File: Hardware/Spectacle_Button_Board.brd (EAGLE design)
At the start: 34.3 x 62.2 mm, 40 parts, among them J19 FTDI_DEVICE, U1 CY8C4146LQI-S422, U2 MIC5205-5V

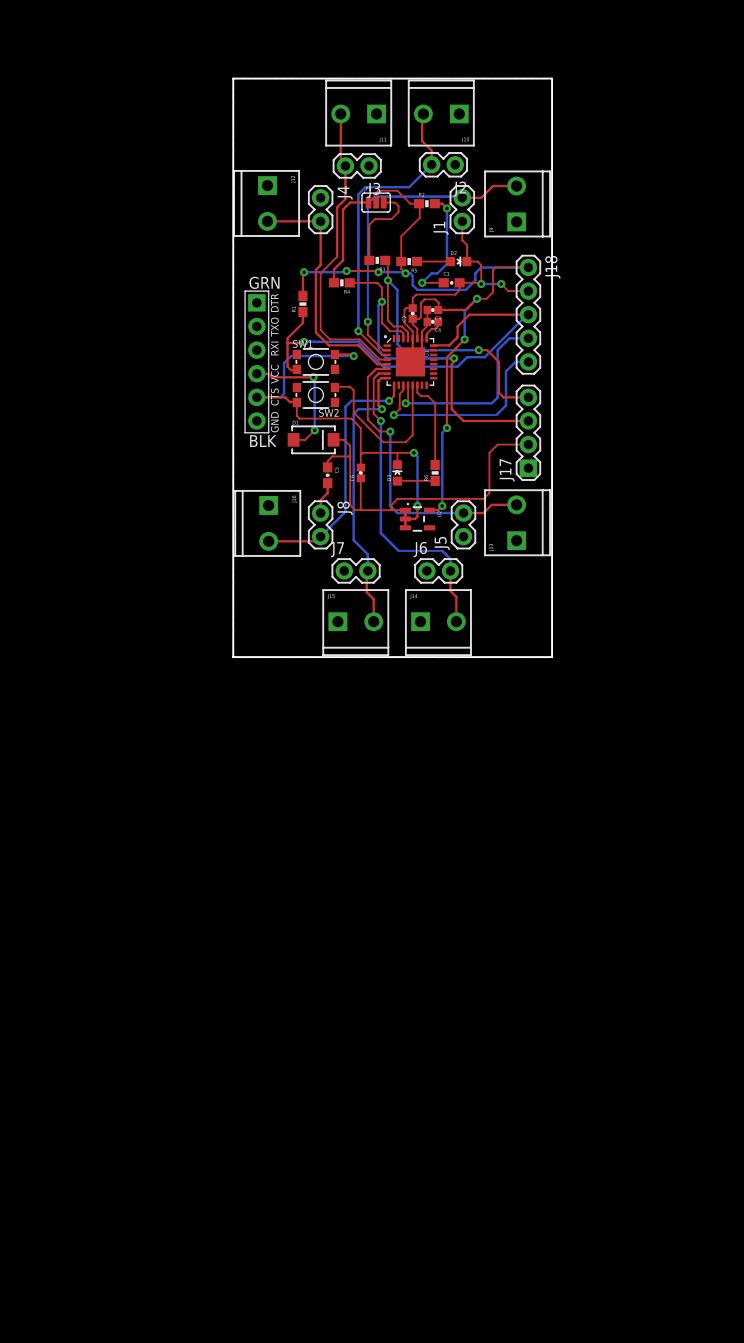
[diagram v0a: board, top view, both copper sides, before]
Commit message: Make some chgs (see full msg) - Add TVS diodes to all button and data/power lines - Partition schematic according to function - Change power/data connector to TRRS
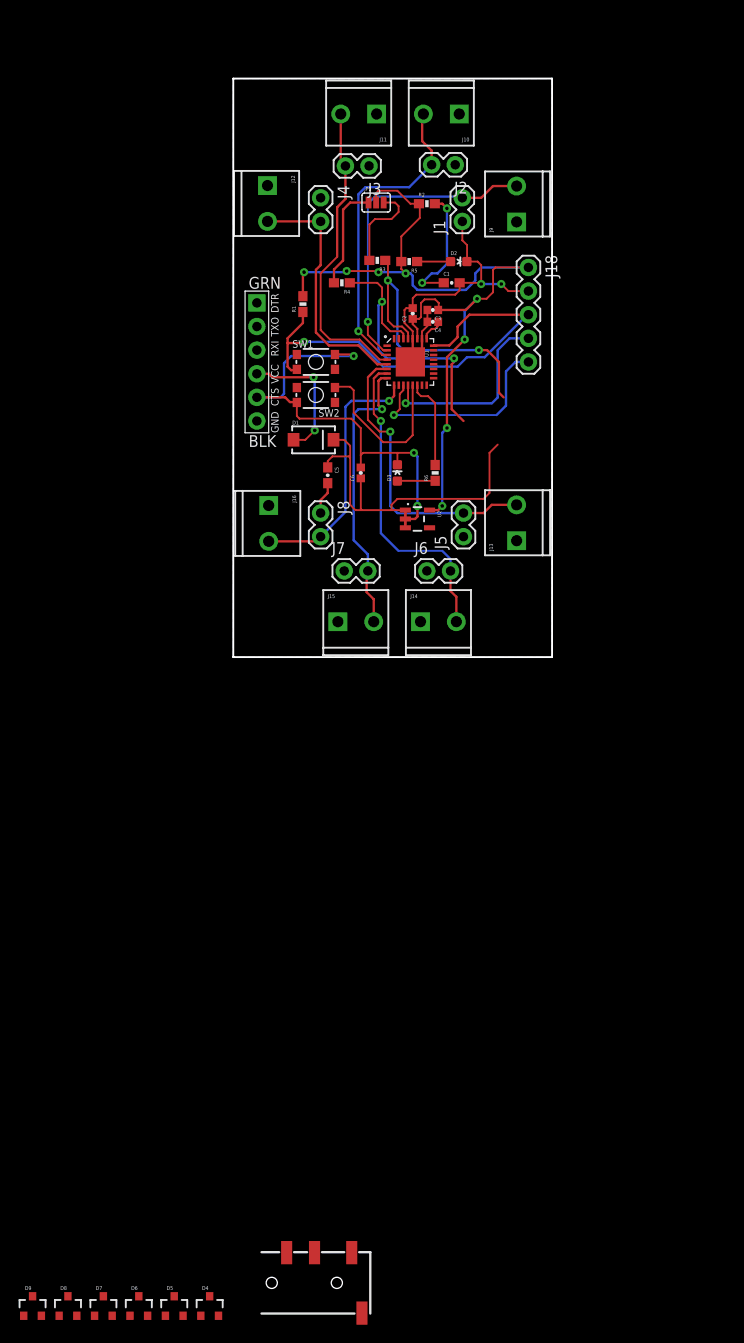
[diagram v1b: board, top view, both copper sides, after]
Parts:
- added D4, D5, D6, D7, D8, D9: PESD1CAN, SparkFun-DiscreteSemi:SOT23-3
- J17: value (none) -> AUDIO-JACK3; device SparkFun-Connectors:1X04 -> SparkFun-Connectors:AUDIO-JACK-TRRS-SMD
- moved J17 92.4 mm to (-24.1, -71.1), turned to 0 degrees
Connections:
- net GND: now also D4.3, D5.3, D6.3, D7.3, D8.3, D9.3, J17.RING2; no longer J17.1
- net IN_0: now also D6.2
- net IN_1: now also D6.1
- net IN_2: now also D8.2
- net IN_3: now also D8.1
- net IN_4: now also D7.2
- net IN_5: now also D7.1
- net IN_6: now also D9.2
- net IN_7: now also D9.1
- net SCL: now also D4.1, J17.RING1; no longer J17.4
- net SDA: now also D4.2, J17.TIP; no longer J17.3
- net VIN: now also D5.1, J17.EARTH; no longer J17.2
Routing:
- net SDA: track 39.0 -> 32.0 mm
- net VIN: track 43.8 -> 40.5 mm
- net SCL: track 35.6 -> 33.0 mm

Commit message: Fix TX and RX net names
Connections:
- removed net RX: U1.21
- removed net TX: U1.22
- net RXI: now also U1.21
- net TXO: now also U1.22
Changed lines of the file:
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@@
 <signal name="TXO">
 <contactref element="J19" pad="P$2"/>
+<contactref element="U1" pad="22"/>
+<wire x1="-24.13" y1="31.75" x2="-5.12" y2="28.69" width="0" layer="19" extent="1-1"/>
 </signal>
 <signal name="RXI">
 <contactref element="J19" pad="P$3"/>
-</signal>
-<signal name="RX">
 <contactref element="U1" pad="21"/>
-</signal>
-<signal name="TX">
-<contactref element="U1" pad="22"/>
+<wire x1="-24.13" y1="29.21" x2="-5.12" y2="28.19" width="0" layer="19" extent="1-1"/>
 </signal>
 <signal name="N$4">

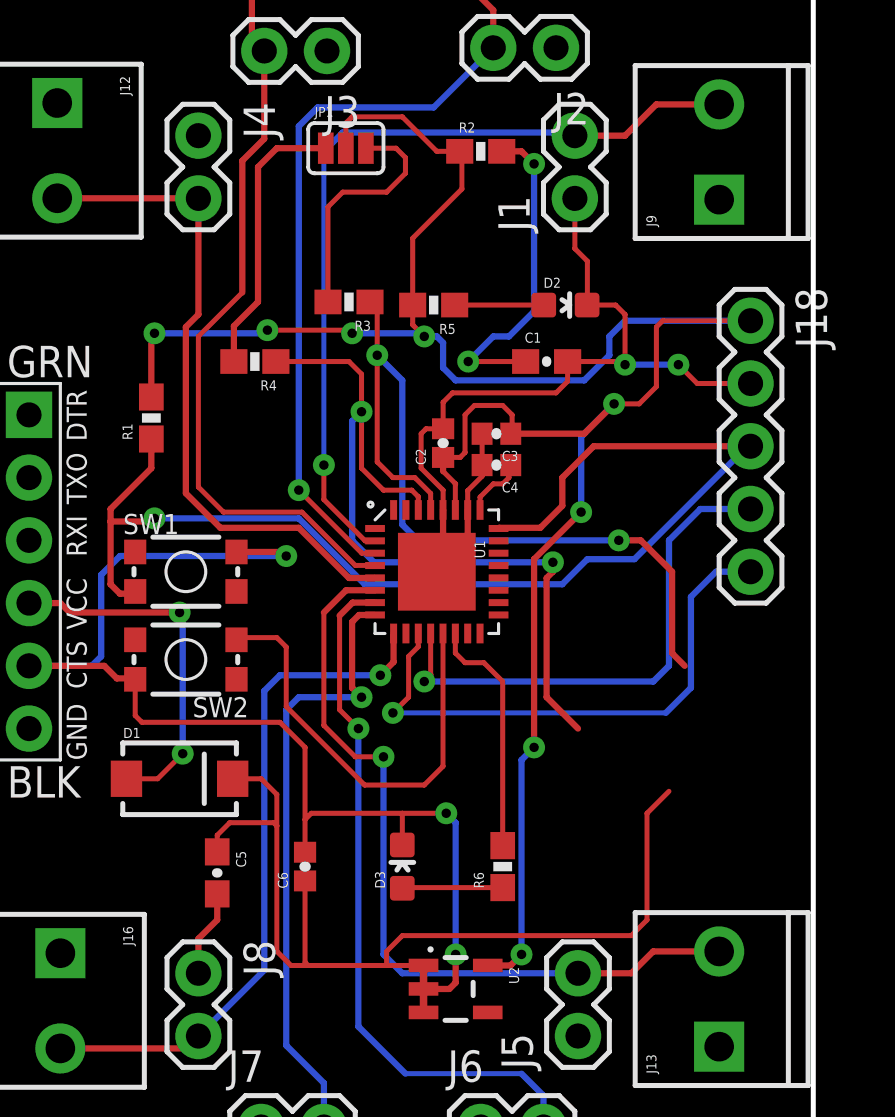
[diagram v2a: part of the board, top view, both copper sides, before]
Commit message: Adjust to 3.3V
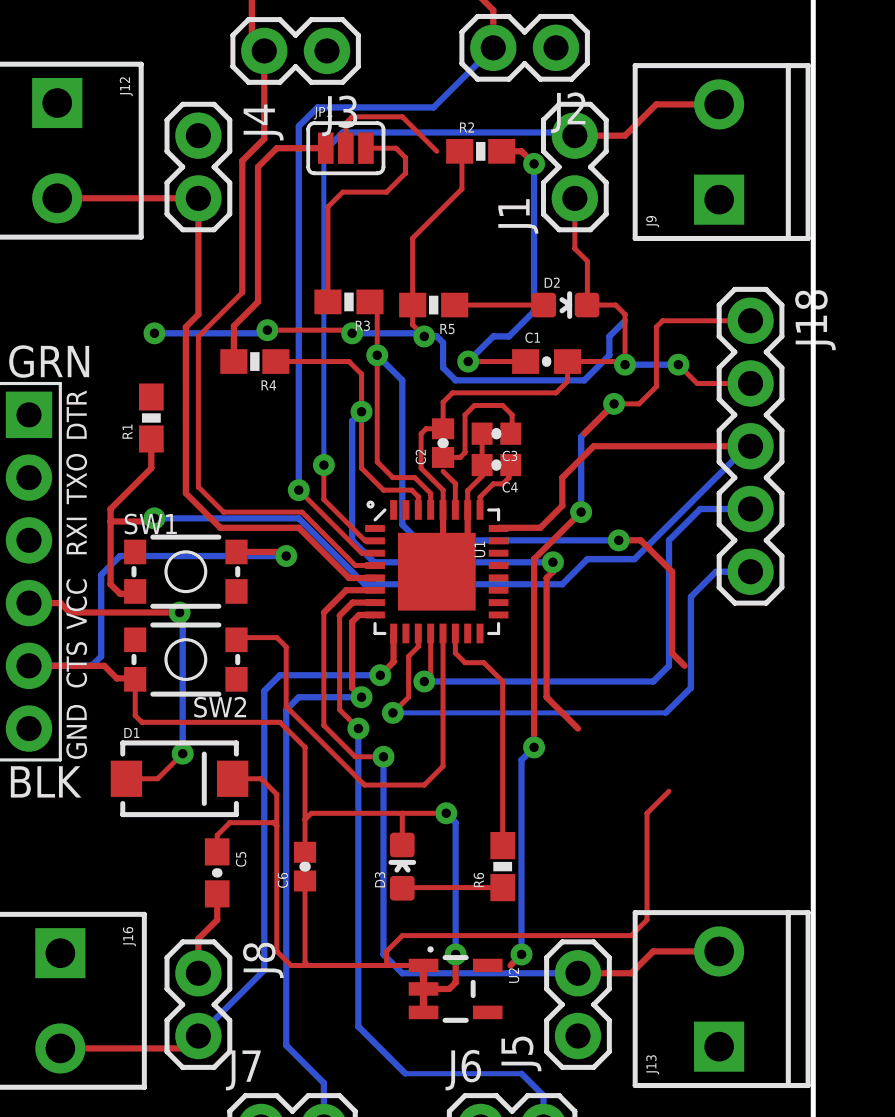
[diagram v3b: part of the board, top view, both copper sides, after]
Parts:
- U2: value MIC5205-5V -> 3.3V/150mA
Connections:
- net 5V renamed 3.3V
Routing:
- net 3.3V: track 90.8 -> 77.8 mm

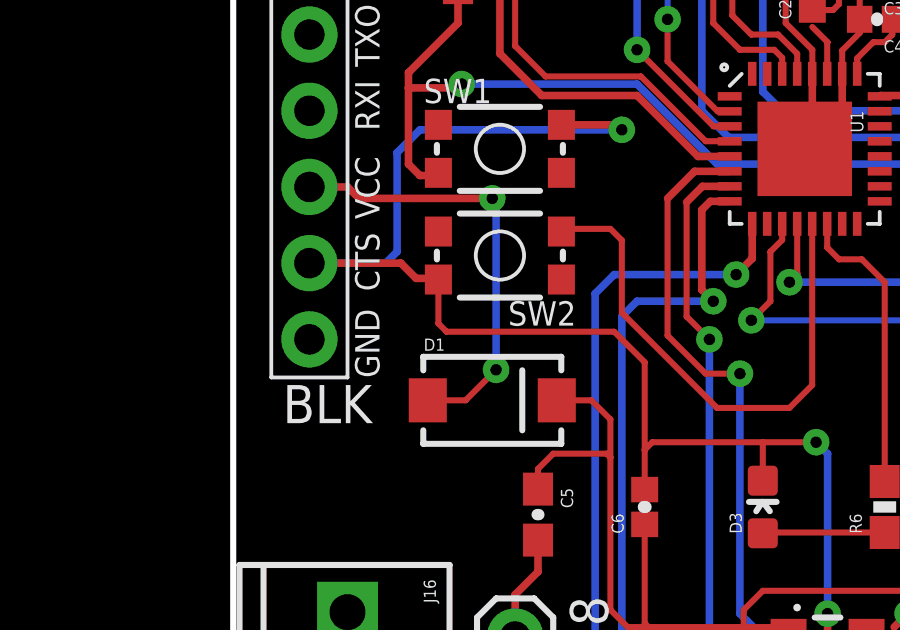
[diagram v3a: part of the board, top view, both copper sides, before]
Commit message: Remove diode from serial port to VIN
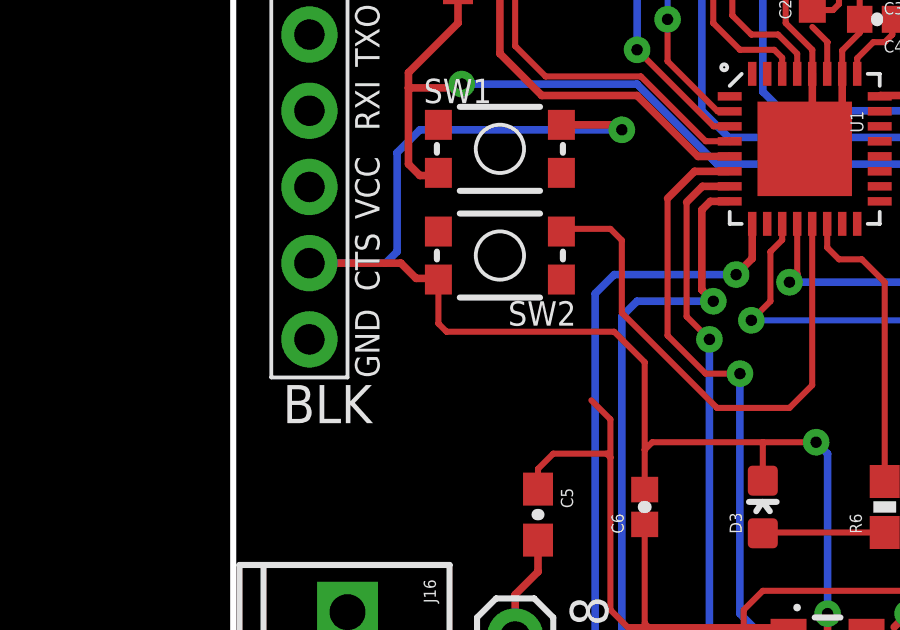
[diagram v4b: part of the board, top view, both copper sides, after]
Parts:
- removed D1: MBRA140, SparkFun-DiscreteSemi:SMA-DIODE
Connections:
- removed net N$1: D1.A, J19.P$4
- net VIN: no longer D1.C
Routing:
- net N$1: track 14.7 -> 0.00 mm, vias 2 -> 0
- net VIN: track 40.5 -> 39.4 mm
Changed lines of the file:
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@@
 <element name="J18" library="SparkFun-Connectors" package="1X05" value="" x="5.08" y="38.1" rot="R270"/>
 <element name="J19" library="SparkFun-Connectors" package="FTDI_DEVICE_SIDE" value="FTDI_DEVICE" x="-24.13" y="27.94" rot="R270"/>
-<element name="D1" library="SparkFun-DiscreteSemi" package="SMA-DIODE" value="MBRA140" x="-18.034" y="19.558">
-<attribute name="PROD_ID" value="DIO-08053" x="-18.034" y="19.558" size="1.778" layer="27" font="vector" ratio="15" display="off"/>
-</element>
 <element name="D2" library="SparkFun-LED" package="LED-0603" value="RED" x="-2.413" y="38.735" rot="R270">
 <attribute name="PROD_ID" value="DIO-00819" x="-2.413" y="38.735" size="1.778" layer="27" font="vector" ratio="15" rot="R270" display="off"/>
@@
 <contactref element="C6" pad="1"/>
 <contactref element="C5" pad="1"/>
-<contactref element="D1" pad="C"/>
 <wire x1="-8.1581" y1="11.999" x2="-8.1581" y2="10.099" width="0.3048" layer="1"/>
-<wire x1="-15.884" y1="19.558" x2="-14.732" y2="19.558" width="0.2032" layer="1"/>
 <wire x1="-14.732" y1="19.558" x2="-14.097" y2="18.923" width="0.2032" layer="1"/>
 <wire x1="-14.097" y1="18.923" x2="-14.097" y2="17.653" width="0.2032" layer="1"/>
@@
 <wire x1="3.048" y1="30.48" x2="5.08" y2="30.48" width="0.254" layer="16"/>
 </signal>
-<signal name="N$1">
-<contactref element="J19" pad="P$4"/>
-<contactref element="D1" pad="A"/>
-<wire x1="-20.184" y1="19.558" x2="-18.923" y2="19.558" width="0.2032" layer="1"/>
-<wire x1="-18.923" y1="19.558" x2="-17.907" y2="20.574" width="0.2032" layer="1"/>
-<via x="-17.907" y="20.574" extent="1-16" drill="0.381"/>
-<wire x1="-17.907" y1="20.574" x2="-17.907" y2="26.162" width="0.254" layer="16"/>
-<wire x1="-17.907" y1="26.162" x2="-18.034" y2="26.289" width="0.254" layer="16"/>
-<via x="-18.034" y="26.289" extent="1-16" drill="0.381"/>
-<wire x1="-18.034" y1="26.289" x2="-22.479" y2="26.289" width="0.254" layer="1"/>
-<wire x1="-22.479" y1="26.289" x2="-22.86" y2="26.67" width="0.254" layer="1"/>
-<wire x1="-22.86" y1="26.67" x2="-24.13" y2="26.67" width="0.254" layer="1"/>
-</signal>
 <signal name="TXO">

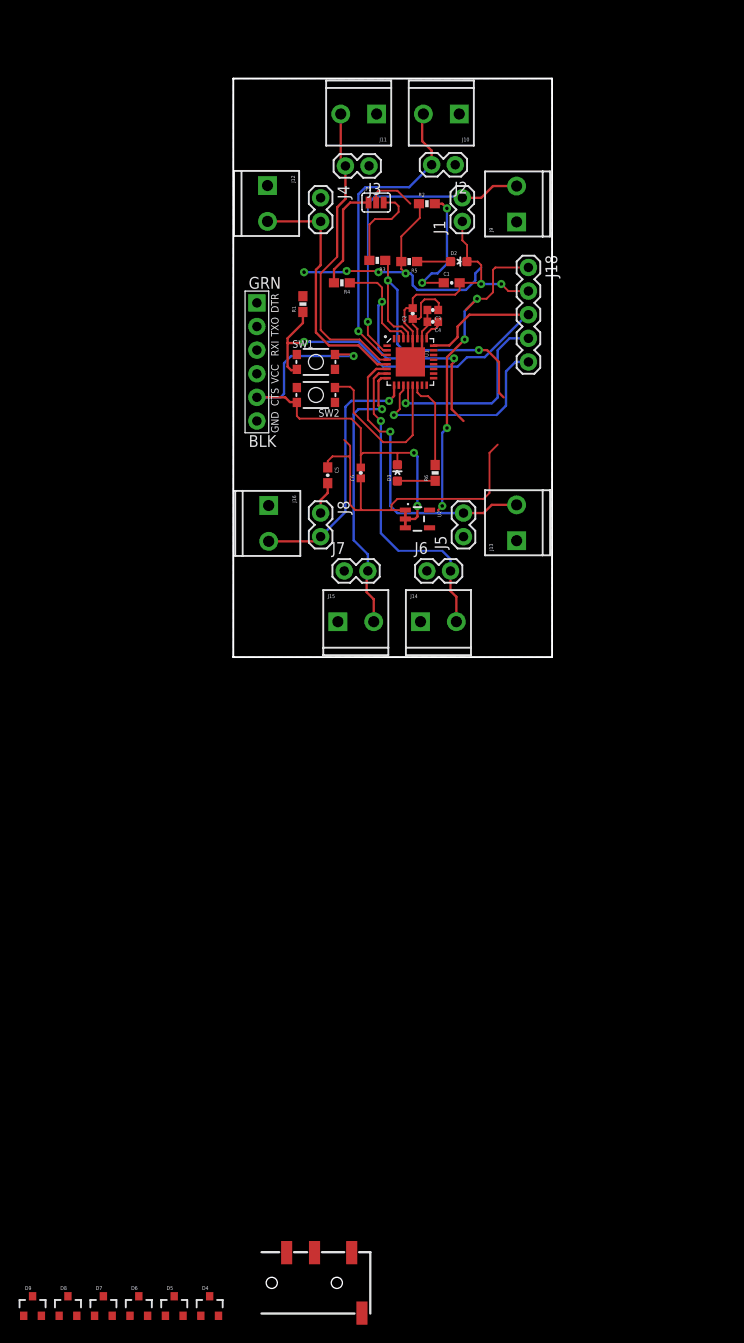
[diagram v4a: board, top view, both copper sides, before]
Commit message: Changed to pokehome connectors
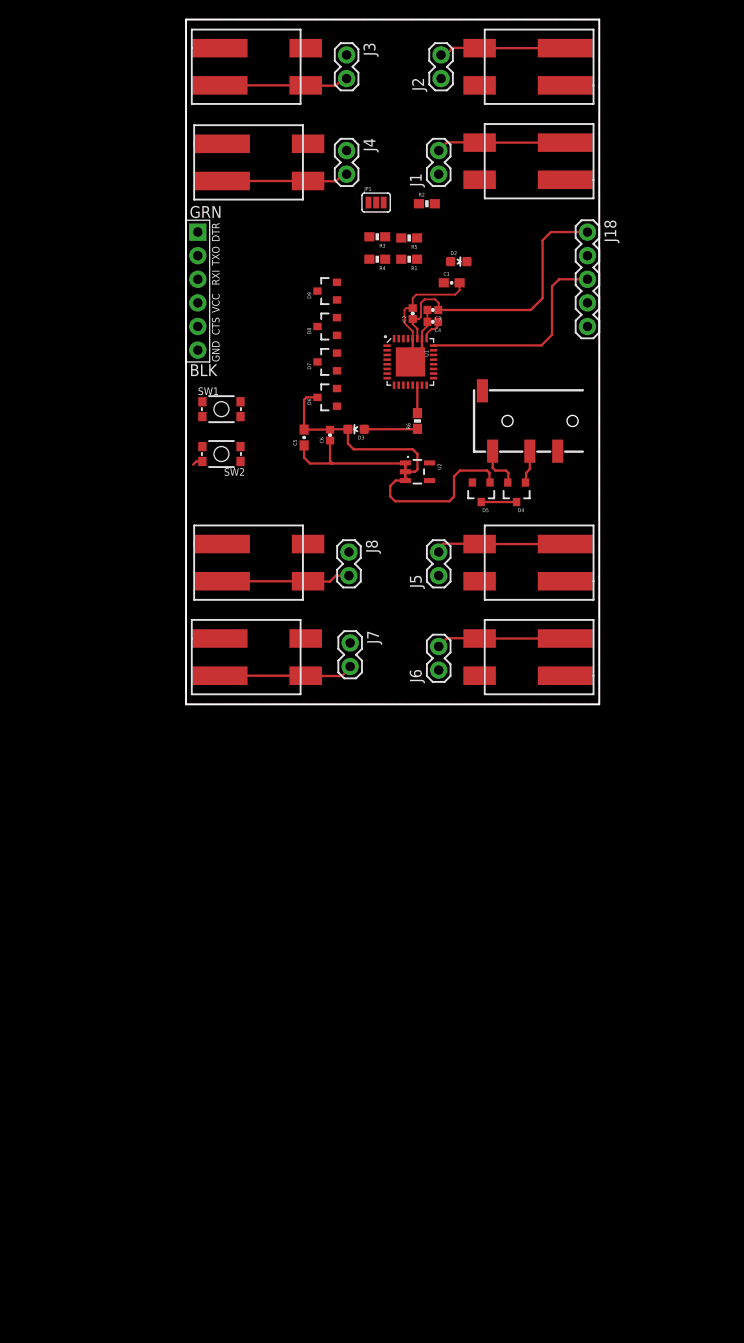
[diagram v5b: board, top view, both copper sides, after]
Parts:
- J10, J11, J12, J13, J14, J15, J16, J9: device SparkFun-Connectors:SCREWTERMINAL-3.5MM-2_LOCK -> SparkFun-Connectors:1X02_POKEHOME
- moved D9 113.7 mm to (-16.5, 35.6), turned to 90 degrees
- moved D8 109.1 mm to (-16.5, 31.8), turned to 90 degrees
- moved D7 104.4 mm to (-16.5, 27.9), turned to 90 degrees
- moved D6 99.9 mm to (-16.5, 24.1), turned to 90 degrees
- moved J17 99.3 mm to (11.4, 21.6), turned to 180 degrees
- moved D4 93.6 mm to (3.81, 14.0), turned to 180 degrees
- moved D5 93.6 mm to (0.00, 14.0), turned to 180 degrees
- moved J11 13.7 mm to (-24.1, 59.7), turned to 0 degrees
- moved R1 12.4 mm to (-7.75, 39.0), turned to 180 degrees
- moved J3 12.2 mm to (-14.5, 61.0), turned to 270 degrees
- moved J14 12.0 mm to (5.08, -3.81), turned to 180 degrees
- moved SW2 12.0 mm to (-27.9, 18.0)
- moved SW1 11.4 mm to (-27.9, 22.9)
- moved J6 10.7 mm to (-4.57, -5.21), turned to 90 degrees
- moved J19 9.92 mm to (-30.5, 35.6)
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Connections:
- net GND: now also J10.P1, J10.P3, J11.P1, J11.P3, J12.P1, J12.P3, J13.P1, J13.P3, J14.P1, J14.P3, J15.P1, J15.P3, J16.P1, J16.P3, J9.P1, J9.P3; no longer J10.1, J11.1, J12.1, J13.1, J14.1, J15.1, J16.1, J9.1
- net IN_0: now also J9.P2, J9.P4; no longer J9.2
- net IN_1: now also J10.P2, J10.P4; no longer J10.2
- net IN_2: now also J11.P2, J11.P4; no longer J11.2
- net IN_3: now also J12.P2, J12.P4; no longer J12.2
- net IN_4: now also J13.P2, J13.P4; no longer J13.2
- net IN_5: now also J14.P2, J14.P4; no longer J14.2
- net IN_6: now also J15.P2, J15.P4; no longer J15.2
- net IN_7: now also J16.P2, J16.P4; no longer J16.2
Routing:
- net 3.3V: track 77.8 -> 31.0 mm, vias 8 -> 0
- net GND: track 90.9 -> 48.8 mm, vias 5 -> 0
- net SCL: track 33.0 -> 3.56 mm, vias 2 -> 0
- net SDA: track 32.0 -> 4.77 mm, vias 2 -> 0
- net XRES: track 49.4 -> 22.6 mm, vias 1 -> 0
- net SWD_DATA: track 22.6 -> 0.00 mm, vias 1 -> 0
- net SWD_CLK: track 21.1 -> 0.00 mm, vias 1 -> 0
- net IN_1: track 34.1 -> 13.7 mm, vias 1 -> 0
- net IN_5: track 34.3 -> 14.0 mm, vias 1 -> 0
- net IN_0: track 33.8 -> 14.0 mm, vias 1 -> 0
- net IN_2: track 33.0 -> 14.0 mm
- net BTN: track 18.0 -> 0.00 mm
- net IN_4: track 32.2 -> 14.3 mm, vias 1 -> 0
- net IN_6: track 30.9 -> 14.5 mm, vias 1 -> 0
- net IN_7: track 27.7 -> 13.9 mm, vias 1 -> 0
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- added copper zone on layer 1, net GND
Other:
- board size 34.3 x 62.2 mm -> 44.5 x 73.7 mm
